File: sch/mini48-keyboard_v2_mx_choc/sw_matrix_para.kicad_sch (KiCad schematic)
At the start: 96 parts, among them SW1 SW_Push, SW10 SW_Push, SW11 SW_Push, SW12 SW_Push, SW13 SW_Push, SW14 SW_Push, SW15 SW_Push, SW16 SW_Push, SW17 SW_Push, SW18 SW_Push, SW19 SW_Push, SW2 SW_Push, SW20 SW_Push, SW21 SW_Push, SW22 SW_Push, SW23 SW_Push, SW24 SW_Push, SW25 SW_Push, SW26 SW_Push, SW27 SW_Push, SW28 SW_Push, SW29 SW_Push, SW3 SW_Push, SW30 SW_Push, SW31 SW_Push, SW32 SW_Push, SW33 SW_Push, SW34 SW_Push, SW35 SW_Push, SW36 SW_Push, SW37 SW_Push, SW38 SW_Push, SW39 SW_Push, SW4 SW_Push, SW40 SW_Push, SW47 SW_Push, SW48 SW_Push, SW5 SW_Push, SW6 SW_Push, SW7 SW_Push, SW8 SW_Push, SW9 SW_Push

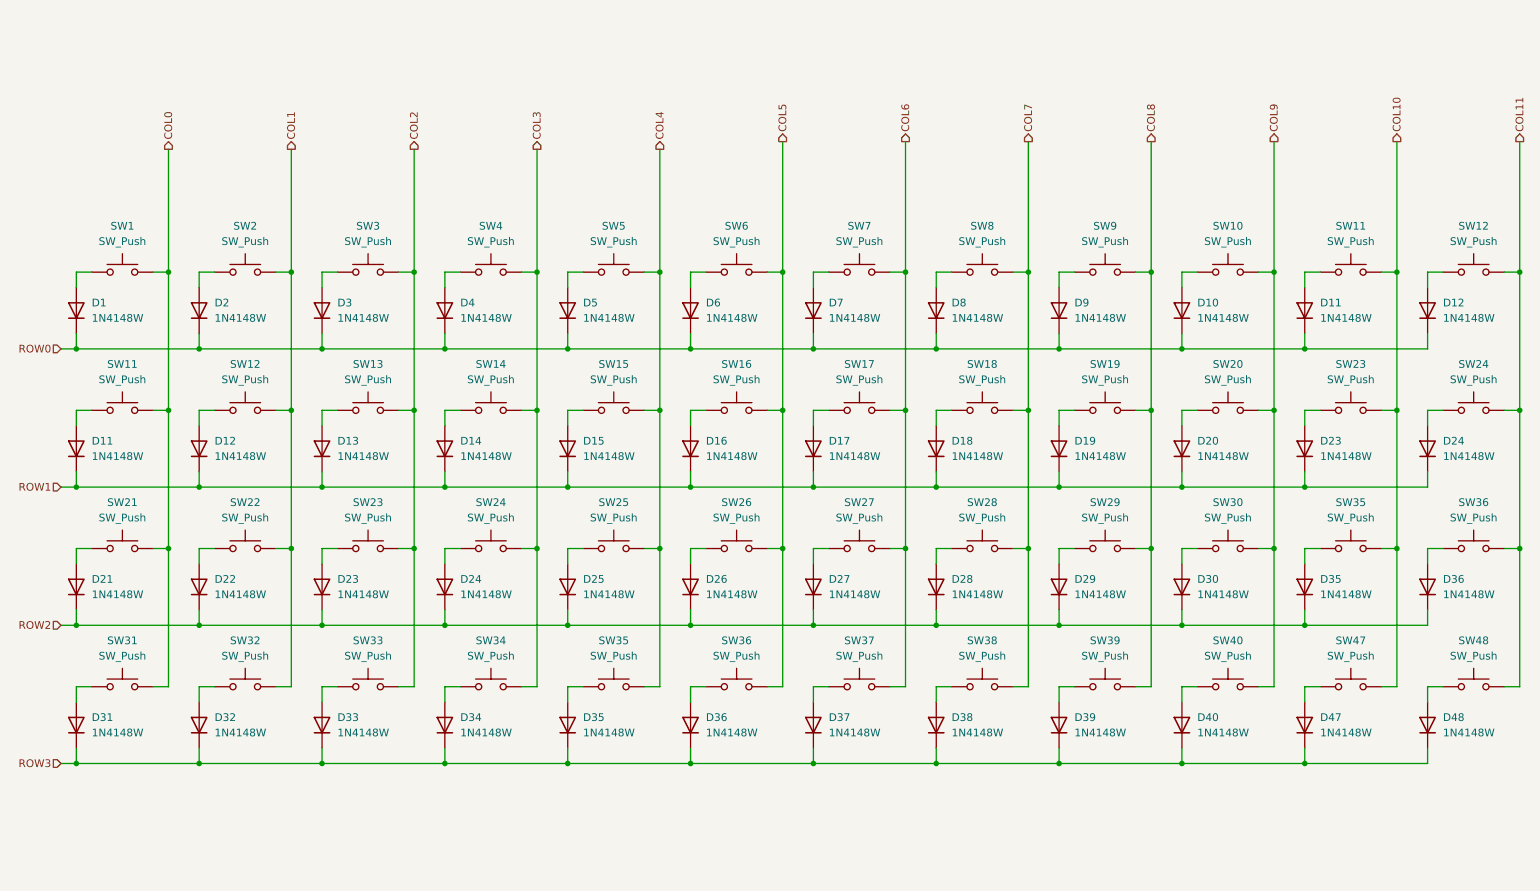
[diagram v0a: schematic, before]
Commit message: MXとchocを並列に接続しました。 基板外形を変更中。
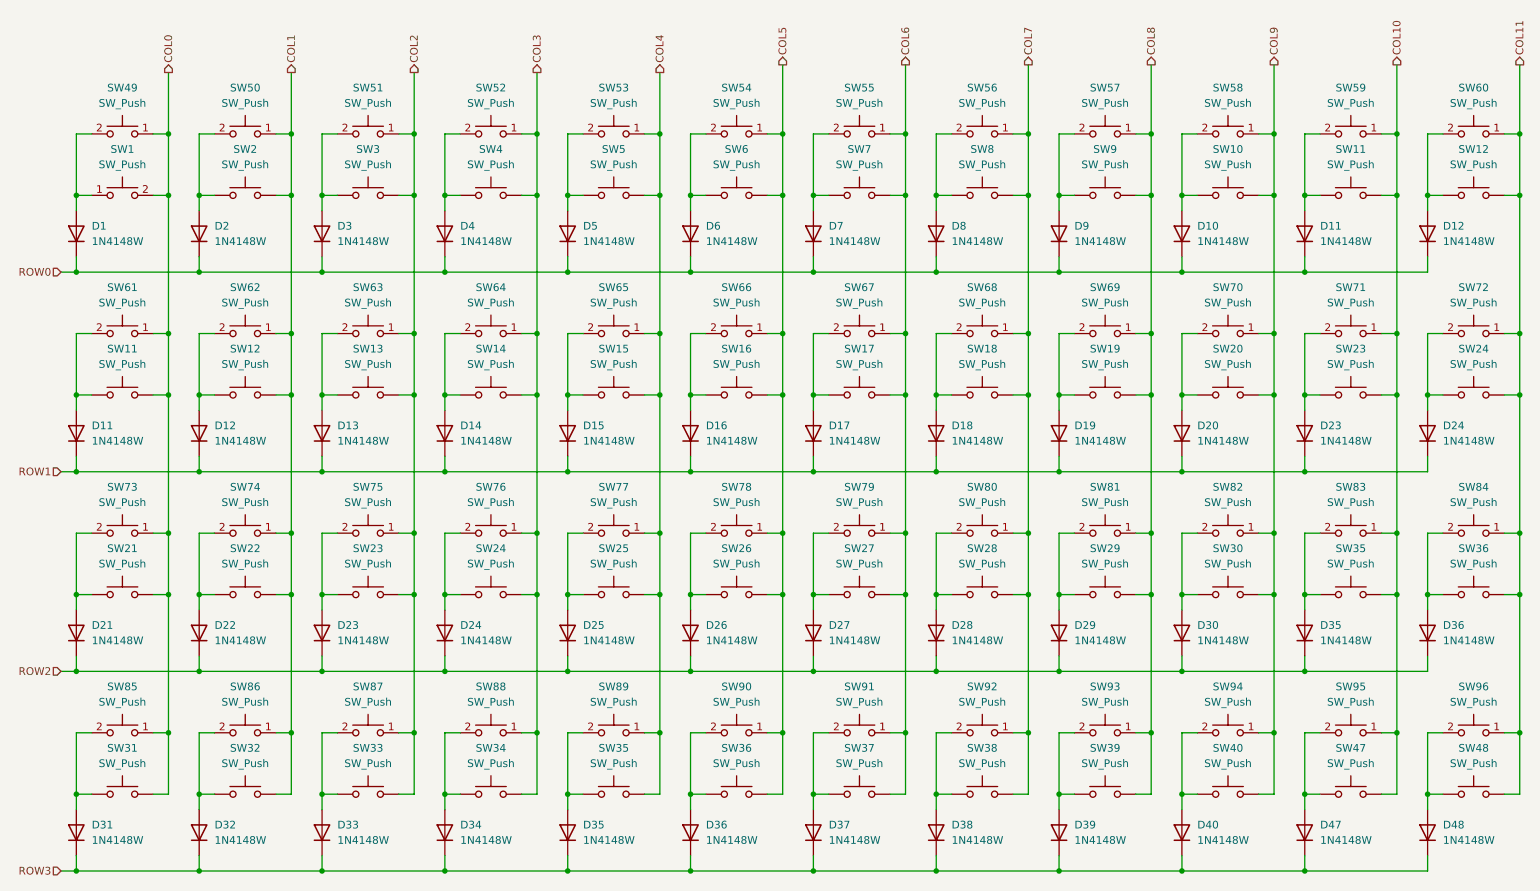
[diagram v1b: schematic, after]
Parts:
- added SW49, SW50, SW51, SW52, SW53, SW54, SW55, SW56, SW57, SW58, SW59, SW60, SW61, SW62, SW63, SW64, SW65, SW66, SW67, SW68, SW69, SW70, SW71, SW72, SW73, SW74, SW75, SW76, SW77, SW78, SW79, SW80, SW81, SW82, SW83, SW84, SW85, SW86, SW87, SW88, SW89, SW90, SW91, SW92, SW93, SW94, SW95, SW96: SW_Push, my_keyswitch:SW_Hotswap_Kailh_MX, symbol Switch:SW_Push
- SW1, SW10, SW11, SW12, SW13, SW14, SW15, SW16, SW17, SW18, SW19, SW2, SW20, SW21, SW22, SW23, SW24, SW25, SW26, SW27, SW28, SW29, SW3, SW30, SW31, SW32, SW33, SW34, SW35, SW36, SW37, SW38, SW39, SW4, SW40, SW47, SW48, SW5, SW6, SW7, SW8, SW9: footprint my_keyswitch:CherryMX_MidHeight_Choc_Hotswap_rev1 -> my_keyswitch:SW_Hotswap_Kailh_Choc_V1V2_no_mp
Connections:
- net COL0: now also SW49.1, SW61.1, SW73.1, SW85.1
- net COL1: now also SW50.1, SW62.1, SW74.1, SW86.1
- net COL10: now also SW59.1, SW71.1, SW83.1, SW95.1
- net COL11: now also SW60.1, SW72.1, SW84.1, SW96.1
- net COL2: now also SW51.1, SW63.1, SW75.1, SW87.1
- net COL3: now also SW52.1, SW64.1, SW76.1, SW88.1
- net COL4: now also SW53.1, SW65.1, SW77.1, SW89.1
- net COL5: now also SW54.1, SW66.1, SW78.1, SW90.1
- net COL6: now also SW55.1, SW67.1, SW79.1, SW91.1
- net COL7: now also SW56.1, SW68.1, SW80.1, SW92.1
- net COL8: now also SW57.1, SW69.1, SW81.1, SW93.1
- net COL9: now also SW58.1, SW70.1, SW82.1, SW94.1
- net at D21.2 (A), SW21.1: now also SW73.2
- net at D4.2 (A), SW4.1: now also SW52.2
- net at D23.2 (A), SW23.1: now also SW75.2
- net at D38.2 (A), SW38.1: now also SW92.2
- net at D32.2 (A), SW32.1: now also SW86.2
- net at D28.2 (A), SW28.1: now also SW80.2
- net at D27.2 (A), SW27.1: now also SW79.2
- net at D18.2 (A), SW18.1: now also SW68.2
- net at D47.2 (A), SW47.1: now also SW95.2
- net at D12.2 (A), SW12.1: now also SW62.2
- net at D3.2 (A), SW3.1: now also SW51.2
- net at D9.2 (A), SW9.1: now also SW57.2
- net at D14.2 (A), SW14.1: now also SW64.2
- net at D37.2 (A), SW37.1: now also SW91.2
- net at D33.2 (A), SW33.1: now also SW87.2
- net at D16.2 (A), SW16.1: now also SW66.2
- net at D31.2 (A), SW31.1: now also SW85.2
- net at D22.2 (A), SW22.1: now also SW74.2
- net at D34.2 (A), SW34.1: now also SW88.2
- net at D7.2 (A), SW7.1: now also SW55.2
- net at D2.2 (A), SW2.1: now also SW50.2
- net at D35.2 (A), SW35.1: now also SW83.2
- net at D11.2 (A), SW11.1: now also SW59.2
- net at D5.2 (A), SW5.1: now also SW53.2
- net at D13.2 (A), SW13.1: now also SW63.2
- net at D15.2 (A), SW15.1: now also SW65.2
- net at D17.2 (A), SW17.1: now also SW67.2
- net at D29.2 (A), SW29.1: now also SW81.2
- net at D36.2 (A), SW36.1: now also SW84.2
- net at D40.2 (A), SW40.1: now also SW94.2
- net at D12.2 (A), SW12.1: now also SW60.2
- net at D10.2 (A), SW10.1: now also SW58.2
- net at D8.2 (A), SW8.1: now also SW56.2
- net at D48.2 (A), SW48.1: now also SW96.2
- net at D11.2 (A), SW11.1: now also SW61.2
- net at D36.2 (A), SW36.1: now also SW90.2
- net at D1.2 (A), SW1.1: now also SW49.2
- net at D19.2 (A), SW19.1: now also SW69.2
- net at D23.2 (A), SW23.1: now also SW71.2
- net at D6.2 (A), SW6.1: now also SW54.2
- net at D35.2 (A), SW35.1: now also SW89.2
- net at D24.2 (A), SW24.1: now also SW76.2
- net at D24.2 (A), SW24.1: now also SW72.2
- net at D25.2 (A), SW25.1: now also SW77.2
- net at D26.2 (A), SW26.1: now also SW78.2
- net at D20.2 (A), SW20.1: now also SW70.2
- net at D30.2 (A), SW30.1: now also SW82.2
- net at D39.2 (A), SW39.1: now also SW93.2
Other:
- moved on the sheet: D1, D10, D11, D12, D13, D14, D15, D16, D17, D18, D19, D2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

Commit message: KiCad のバージョンを9に上げました。
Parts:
- renumbered D11 to D13, D12 to D14, D13 to D15, D14 to D16, D15 to D17, D16 to D18, D17 to D19, D18 to D20, D19 to D21, D20 to D22, D21 to D25, D22 to D26, D23 to D27, D24 to D28, D25 to D29, D26 to D30, D27 to D31, D28 to D32, D29 to D33, D30 to D34, D31 to D37, D32 to D38, D33 to D39, D34 to D40, D35 to D41, D36 to D42, D37 to D43, D38 to D44, D39 to D45, D40 to D46, SW11 to SW13, SW12 to SW14, SW13 to SW15, SW14 to SW16, SW15 to SW17, SW16 to SW18, SW17 to SW19, SW18 to SW20, SW19 to SW21, SW20 to SW22, SW21 to SW25, SW22 to SW26, SW23 to SW27, SW24 to SW28, SW25 to SW29, SW26 to SW30, SW27 to SW31, SW28 to SW32, SW29 to SW33, SW30 to SW34, SW31 to SW37, SW32 to SW38, SW33 to SW39, SW34 to SW40, SW35 to SW41, SW36 to SW42, SW37 to SW43, SW38 to SW44, SW39 to SW45, SW40 to SW46
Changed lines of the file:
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@@
 (kicad_sch
-	(version 20231120)
+	(version 20250114)
 	(generator "eeschema")
-	(generator_version "8.0")
+	(generator_version "9.0")
 	(paper "A4")
 	(junction
@@
 		(dnp no)
 		(fields_autoplaced yes)
-		(property "Reference" "SW21"
+		(property "Reference" "SW25"
 			(at 34.29 101.6 0)
 			(effects
@@
 		(dnp no)
 		(fields_autoplaced yes)
-		(property "Reference" "D23"
+		(property "Reference" "D27"
 			(at 69.85 114.3 90)
 			(effects
@@
 		(dnp no)
 		(fields_autoplaced yes)
-		(property "Reference" "SW38"
+		(property "Reference" "SW44"
 			(at 176.53 134.62 0)
 			(effects
@@
 		(dnp no)
 		(fields_autoplaced yes)
-		(property "Reference" "SW32"
+		(property "Reference" "SW38"
 			(at 54.61 134.62 0)
 			(effects
@@
 		(dnp no)
 		(fields_autoplaced yes)
-		(property "Reference" "SW28"
+		(property "Reference" "SW32"
 			(at 176.53 101.6 0)
 			(effects
@@
 		(dnp no)
 		(fields_autoplaced yes)
-		(property "Reference" "SW27"
+		(property "Reference" "SW31"
 			(at 156.21 101.6 0)
 			(effects
@@
 		(dnp no)
 		(fields_autoplaced yes)
-		(property "Reference" "SW18"
+		(property "Reference" "SW20"
 			(at 176.53 68.58 0)
 			(effects
@@
 		(dnp no)
 		(fields_autoplaced yes)
-		(property "Reference" "D12"
+		(property "Reference" "D14"
 			(at 49.53 81.28 90)
 			(effects
@@
 		(dnp no)
 		(fields_autoplaced yes)
-		(property "Reference" "D14"
+		(property "Reference" "D16"
 			(at 90.17 81.28 90)
 			(effects
@@
 		(dnp no)
 		(fields_autoplaced yes)
-		(property "Reference" "SW37"
+		(property "Reference" "SW43"
 			(at 156.21 134.62 0)
 			(effects
@@
 		(dnp no)
 		(fields_autoplaced yes)
-		(property "Reference" "D28"
+		(property "Reference" "D32"
 			(at 171.45 114.3 90)
 			(effects
@@
 		(dnp no)
 		(fields_autoplaced yes)
-		(property "Reference" "SW33"
+		(property "Reference" "SW39"
 			(at 74.93 134.62 0)
 			(effects
@@
 		(dnp no)
 		(fields_autoplaced yes)
-		(property "Reference" "D16"
+		(property "Reference" "D18"
 			(at 130.81 81.28 90)
 			(effects
@@
 		(dnp no)
 		(fields_autoplaced yes)
-		(property "Reference" "SW31"
+		(property "Reference" "SW37"
 			(at 34.29 134.62 0)
 			(effects
@@
 		(dnp no)
 		(fields_autoplaced yes)
-		(property "Reference" "D21"
+		(property "Reference" "D25"
 			(at 29.21 114.3 90)
 			(effects
@@
 		(dnp no)
 		(fields_autoplaced yes)
-		(property "Reference" "SW22"
+		(property "Reference" "SW26"
 			(at 54.61 101.6 0)
 			(effects
@@
 		(dnp no)
 		(fields_autoplaced yes)
-		(property "Reference" "SW34"
+		(property "Reference" "SW40"
 			(at 95.25 134.62 0)
 			(effects
@@
 		(dnp no)
 		(fields_autoplaced yes)
-		(property "Reference" "SW13"
+		(property "Reference" "SW15"
 			(at 74.93 68.58 0)
 			(effects
@@
 		(dnp no)
 		(fields_autoplaced yes)
-		(property "Reference" "D15"
+		(property "Reference" "D17"
 			(at 110.49 81.28 90)
 			(effects
@@
 		(dnp no)
 		(fields_autoplaced yes)
-		(property "Reference" "D27"
+		(property "Reference" "D31"
 			(at 151.13 114.3 90)
 			(effects
@@
 		(dnp no)
 		(fields_autoplaced yes)
-		(property "Reference" "SW17"
+		(property "Reference" "SW19"
 			(at 156.21 68.58 0)
 			(effects
@@
 		(dnp no)
 		(fields_autoplaced yes)
-		(property "Reference" "D29"
+		(property "Reference" "D33"
 			(at 191.77 114.3 90)
 			(effects
@@
 		(dnp no)
 		(fields_autoplaced yes)
-		(property "Reference" "SW40"
+		(property "Reference" "SW46"
 			(at 217.17 134.62 0)
 			(effects
@@
 		(dnp no)
 		(fields_autoplaced yes)
-		(property "Reference" "D11"
+		(property "Reference" "D13"
 			(at 29.21 81.28 90)
 			(effects
@@
 		(dnp no)
 		(fields_autoplaced yes)
-		(property "Reference" "SW36"
+		(property "Reference" "SW42"
 			(at 135.89 134.62 0)
 			(effects
@@
 		(dnp no)
 		(fields_autoplaced yes)
-		(property "Reference" "D32"
+		(property "Reference" "D38"
 			(at 49.53 147.32 90)
 			(effects
@@
 		(dnp no)
 		(fields_autoplaced yes)
-		(property "Reference" "D36"
+		(property "Reference" "D42"
 			(at 130.81 147.32 90)
 			(effects
@@
 		(dnp no)
 		(fields_autoplaced yes)
-		(property "Reference" "D40"
+		(property "Reference" "D46"
 			(at 212.09 147.32 90)
 			(effects
@@
 		(dnp no)
 		(fields_autoplaced yes)
-		(property "Reference" "SW19"
+		(property "Reference" "SW21"
 			(at 196.85 68.58 0)
 			(effects
@@
 		(dnp no)
 		(fields_autoplaced yes)
-		(property "Reference" "SW35"
+		(property "Reference" "SW41"
 			(at 115.57 134.62 0)
 			(effects
@@
 		(dnp no)
 		(fields_autoplaced yes)
-		(property "Reference" "D13"
+		(property "Reference" "D15"
 			(at 69.85 81.28 90)
 			(effects
@@
 		(dnp no)
 		(fields_autoplaced yes)
-		(property "Reference" "D22"
+		(property "Reference" "D26"
 			(at 49.53 114.3 90)
 			(effects
@@
 		(dnp no)
 		(fields_autoplaced yes)
-		(property "Reference" "D24"
+		(property "Reference" "D28"
 			(at 90.17 114.3 90)
 			(effects
@@
 		(dnp no)
 		(fields_autoplaced yes)
-		(property "Reference" "SW29"
+		(property "Reference" "SW33"
 			(at 196.85 101.6 0)
 			(effects
@@
 		(dnp no)
 		(fields_autoplaced yes)
-		(property "Reference" "D33"
+		(property "Reference" "D39"
 			(at 69.85 147.32 90)
 			(effects
@@
 		(dnp no)
 		(fields_autoplaced yes)
-		(property "Reference" "SW25"
+		(property "Reference" "SW29"
 			(at 115.57 101.6 0)
 			(effects
@@
 		(dnp no)
 		(fields_autoplaced yes)
-		(property "Reference" "SW23"
+		(property "Reference" "SW27"
 			(at 74.93 101.6 0)
 			(effects
@@
 		(dnp no)
 		(fields_autoplaced yes)
-		(property "Reference" "SW15"
+		(property "Reference" "SW17"
 			(at 115.57 68.58 0)
 			(effects
@@
 		(dnp no)
 		(fields_autoplaced yes)
-		(property "Reference" "SW26"
+		(property "Reference" "SW30"
 			(at 135.89 101.6 0)
 			(effects
@@
 		(dnp no)
 		(fields_autoplaced yes)
-		(property "Reference" "D34"
+		(property "Reference" "D40"
 			(at 90.17 147.32 90)
 			(effects
@@
 		(dnp no)
 		(fields_autoplaced yes)
-		(property "Reference" "SW20"
+		(property "Reference" "SW22"
 			(at 217.17 68.58 0)
 			(effects
@@
 		(dnp no)
 		(fields_autoplaced yes)
-		(property "Reference" "SW30"
+		(property "Reference" "SW34"
 			(at 217.17 101.6 0)
 			(effects
@@
 		(dnp no)
 		(fields_autoplaced yes)
-		(property "Reference" "SW16"
+		(property "Reference" "SW18"
 			(at 135.89 68.58 0)
 			(effects
@@
 		(dnp no)
 		(fields_autoplaced yes)
-		(property "Reference" "D35"
+		(property "Reference" "D41"
 			(at 110.49 147.32 90)
 			(effects
@@
 		(dnp no)
 		(fields_autoplaced yes)
-		(property "Reference" "D25"
+		(property "Reference" "D29"
 			(at 110.49 114.3 90)
 			(effects
@@
 		(dnp no)
 		(fields_autoplaced yes)
-		(property "Reference" "D20"
+		(property "Reference" "D22"
 			(at 212.09 81.28 90)
 			(effects
@@
 		(dnp no)
 		(fields_autoplaced yes)
-		(property "Reference" "D37"
+		(property "Reference" "D43"
 			(at 151.13 147.32 90)
 			(effects
@@
 		(dnp no)
 		(fields_autoplaced yes)
-		(property "Reference" "D18"
+		(property "Reference" "D20"
 			(at 171.45 81.28 90)
 			(effects
@@
 		(dnp no)
 		(fields_autoplaced yes)
-		(property "Reference" "D39"
+		(property "Reference" "D45"
 			(at 191.77 147.32 90)
 			(effects
@@
 		(dnp no)
 		(fields_autoplaced yes)
-		(property "Reference" "D26"
+		(property "Reference" "D30"
 			(at 130.81 114.3 90)
 			(effects
@@
 		(dnp no)
 		(fields_autoplaced yes)
-		(property "Reference" "SW24"
+		(property "Reference" "SW28"
 			(at 95.25 101.6 0)
 			(effects
@@
 		(dnp no)
 		(fields_autoplaced yes)
-		(property "Reference" "SW39"
+		(property "Reference" "SW45"
 			(at 196.85 134.62 0)
 			(effects
@@
 		(dnp no)
 		(fields_autoplaced yes)
-		(property "Reference" "D19"
+		(property "Reference" "D21"
 			(at 191.77 81.28 90)
 			(effects
@@
 		(dnp no)
 		(fields_autoplaced yes)
-		(property "Reference" "SW11"
+		(property "Reference" "SW13"
 			(at 34.29 68.58 0)
 			(effects
@@
 		(dnp no)
 		(fields_autoplaced yes)
-		(property "Reference" "D31"
+		(property "Reference" "D37"
 			(at 29.21 147.32 90)
 			(effects
@@
 		(dnp no)
 		(fields_autoplaced yes)
-		(property "Reference" "SW12"
+		(property "Reference" "SW14"
 			(at 54.61 68.58 0)
 			(effects
@@
 		(dnp no)
 		(fields_autoplaced yes)
-		(property "Reference" "SW14"
+		(property "Reference" "SW16"
 			(at 95.25 68.58 0)
 			(effects
@@
 		(dnp no)
 		(fields_autoplaced yes)
-		(property "Reference" "D17"
+		(property "Reference" "D19"
 			(at 151.13 81.28 90)
 			(effects
@@
 		(dnp no)
 		(fields_autoplaced yes)
-		(property "Reference" "D30"
+		(property "Reference" "D34"
 			(at 212.09 114.3 90)
 			(effects
@@
 		(dnp no)
 		(fields_autoplaced yes)
-		(property "Reference" "D38"
+		(property "Reference" "D44"
 			(at 171.45 147.32 90)
 			(effects
